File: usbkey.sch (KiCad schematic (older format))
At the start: 15 parts, among them P1 USART0, P2 DEBUG, P3 USB_B, U1 EFM32HG309

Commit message: Give all the nets names.
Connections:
- net LED1: now reaches R1.1, U1.1 (PA0)
- net DEC: now reaches C1.2, U1.14 (DECOUPLE)
- net RUSB_D+: now reaches R3.2, U1.17 (PC14)
- net RUSB_D-: now reaches R4.2, U1.18 (PC15)
- net CAP1: now reaches U1.23 (PE12), U1.4 (PC1), W2.2
- net CAP0: now reaches U1.24 (PE13), U1.3 (PC0), W1.2
- net US0_TX: now reaches P1.3 (P3), U1.5 (PB7)
- net US0_RX: now reaches P1.2 (P2), U1.6 (PB8)
- net LED0: now reaches R2.2, U1.8 (PB11)
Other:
- note removed: "US0_RX"
- note removed: "US0_TX\n"
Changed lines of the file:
@@
 EESchema Schematic File Version 2
+LIBS:usbkey-rescue
 LIBS:power
 LIBS:device
@@
 P 5725 4025
 F 0 "C1" V 5675 4075 50  0000 L CNN
-F 1 "1uF" V 5675 3850 50  0000 L CNN
+F 1 "1uF" V 5775 4075 50  0000 L CNN
 F 2 "Capacitors_SMD:C_0402" H 5725 4025 50  0001 C CNN
 F 3 "" H 5725 4025 50  0000 C CNN
@@
 	1    0    0    -1
 $EndComp
-Text Notes 2450 3075 0    39   ~ 0
-US0_TX\n
-Text Notes 2450 3175 0    39   ~ 0
-US0_RX
 Wire Wire Line
 	4175 3025 4200 3025
@@
 	4025 3775 4200 3775
 Connection ~ 4025 3625
+Text Label 3850 3425 0    39   ~ 0
+CAP0
+Text Label 3850 3625 0    39   ~ 0
+CAP1
+Text Label 2775 3075 0    39   ~ 0
+US0_TX
+Text Label 2775 3175 0    39   ~ 0
+US0_RX
+Text Label 5550 4025 0    39   ~ 0
+DEC
+Text Label 4175 2600 1    39   ~ 0
+LED1
+Text Label 4050 2600 1    39   ~ 0
+LED0
+Text Label 5500 3100 0    8    ~ 0
+RUSB_D+
+Text Label 5500 3175 0    8    ~ 0
+RUSB_D-
 $EndSCHEMATC

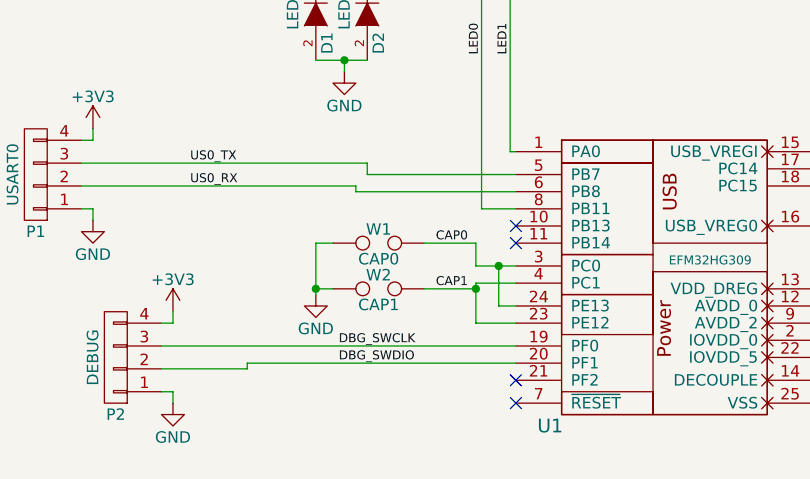
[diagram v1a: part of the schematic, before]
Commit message: Playing with things.
ADC on one side, capacitive on the other.

Starting on USB PCB component.
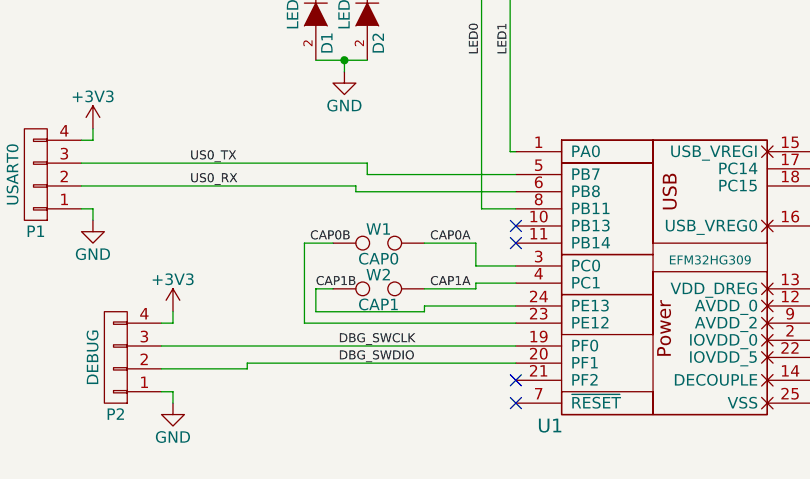
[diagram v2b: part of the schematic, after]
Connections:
- net GND: no longer W1.1, W2.1
- net CAP0 renamed CAP0A
- net CAP0A: no longer U1.24 (PE13)
- net CAP1 renamed CAP1A
- net CAP1A: no longer U1.23 (PE12)
- new net CAP0B: U1.23 (PE12), W1.1
- new net CAP1B: U1.24 (PE13), W2.1
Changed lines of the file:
@@
 $EndComp
 $Comp
-L GND #PWR8
+L GND #PWR01
 U 1 1 5798BA02
 P 6200 4175
-F 0 "#PWR8" H 6200 3925 50  0001 C CNN
+F 0 "#PWR01" H 6200 3925 50  0001 C CNN
 F 1 "GND" H 6200 4025 50  0000 C CNN
 F 2 "" H 6200 4175 50  0000 C CNN
@@
 	2700 4075 2700 4125
 $Comp
-L GND #PWR4
+L GND #PWR02
 U 1 1 5798EEB6
 P 2700 4125
-F 0 "#PWR4" H 2700 3875 50  0001 C CNN
+F 0 "#PWR02" H 2700 3875 50  0001 C CNN
 F 1 "GND" H 2700 3975 50  0000 C CNN
 F 2 "" H 2700 4125 50  0000 C CNN
@@
 	2700 3775 2700 3725
 $Comp
-L +3V3 #PWR7
+L +3V3 #PWR03
 U 1 1 5798EF1D
 P 6000 3575
-F 0 "#PWR7" H 6000 3425 50  0001 C CNN
+F 0 "#PWR03" H 6000 3425 50  0001 C CNN
 F 1 "+3V3" H 6000 3715 50  0000 C CNN
 F 2 "" H 6000 3575 50  0000 C CNN
@@
 Connection ~ 6350 4125
 $Comp
-L +3V3 #PWR3
+L +3V3 #PWR04
 U 1 1 5798F04E
 P 2700 3725
-F 0 "#PWR3" H 2700 3575 50  0001 C CNN
+F 0 "#PWR04" H 2700 3575 50  0001 C CNN
 F 1 "+3V3" H 2700 3865 50  0000 C CNN
 F 2 "" H 2700 3725 50  0000 C CNN
@@
 $EndComp
 $Comp
-L GND #PWR6
+L GND #PWR05
 U 1 1 5798FAA2
 P 3450 2675
-F 0 "#PWR6" H 3450 2425 50  0001 C CNN
+F 0 "#PWR05" H 3450 2425 50  0001 C CNN
 F 1 "GND" H 3450 2525 50  0000 C CNN
 F 2 "" H 3450 2675 50  0000 C CNN
@@
 	2350 3275 2350 3325
 $Comp
-L GND #PWR2
+L GND #PWR06
 U 1 1 5798FD6B
 P 2350 3325
-F 0 "#PWR2" H 2350 3075 50  0001 C CNN
+F 0 "#PWR06" H 2350 3075 50  0001 C CNN
 F 1 "GND" H 2350 3175 50  0000 C CNN
 F 2 "" H 2350 3325 50  0000 C CNN
@@
 	2350 2975 2350 2925
 $Comp
-L +3V3 #PWR1
+L +3V3 #PWR07
 U 1 1 5798FD73
 P 2350 2925
-F 0 "#PWR1" H 2350 2775 50  0001 C CNN
+F 0 "#PWR07" H 2350 2775 50  0001 C CNN
 F 1 "+3V3" H 2350 3065 50  0000 C CNN
 F 2 "" H 2350 2925 50  0000 C CNN
@@
 	1    0    0    -1
 $EndComp
-$Comp
-L GND #PWR5
-U 1 1 57990607
-P 3325 3650
-F 0 "#PWR5" H 3325 3400 50  0001 C CNN
-F 1 "GND" H 3325 3500 50  0000 C CNN
-F 2 "" H 3325 3650 50  0000 C CNN
-F 3 "" H 3325 3650 50  0000 C CNN
-	1    3325 3650
-	1    0    0    -1
-$EndComp
-Wire Wire Line
-	3325 3425 3325 3650
 Wire Wire Line
 	3325 3625 3400 3625
 Wire Wire Line
-	3325 3425 3400 3425
-Connection ~ 3325 3625
+	3275 3425 3400 3425
 Wire Wire Line
 	3800 3425 4025 3425
@@
 Wire Wire Line
 	4200 3600 4025 3600
-Wire Wire Line
-	4025 3600 4025 3775
 Wire Wire Line
 	4025 3625 3800 3625
@@
 NoConn ~ 4200 3350
 Wire Wire Line
-	4200 3700 4125 3700
-Wire Wire Line
-	4125 3700 4125 3525
-Connection ~ 4125 3525
-Wire Wire Line
-	4025 3775 4200 3775
-Connection ~ 4025 3625
-Text Label 3850 3425 0    39   ~ 0
-CAP0
-Text Label 3850 3625 0    39   ~ 0
-CAP1
+	3800 3700 4200 3700
+Wire Wire Line
+	3275 3775 4200 3775
+Text Label 3825 3425 0    39   ~ 0
+CAP0A
+Text Label 3825 3625 0    39   ~ 0
+CAP1A
 Text Label 2775 3075 0    39   ~ 0
 US0_TX
@@
 Text Label 5500 3175 0    8    ~ 0
 RUSB_D-
+Wire Wire Line
+	4025 3600 4025 3625
+Wire Wire Line
+	3800 3700 3800 3725
+Wire Wire Line
+	3800 3725 3325 3725
+Wire Wire Line
+	3325 3725 3325 3625
+Wire Wire Line
+	3275 3775 3275 3425
+Text Label 3300 3425 0    39   ~ 0
+CAP0B
+Text Label 3325 3625 0    39   ~ 0
+CAP1B
 $EndSCHEMATC

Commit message: Temp commit.
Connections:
- net DBG_SWCLK: now also P2.2 (P2); no longer P2.3 (P3)
- net DBG_SWDIO: now also P2.3 (P3); no longer P2.2 (P2)
- net GND: no longer P3.5 (shield)
- net RUSB_D+: now also R4.2, U1.18 (PC15); no longer R3.2, U1.17 (PC14)
- net RUSB_D-: now also R3.2, U1.17 (PC14); no longer R4.2, U1.18 (PC15)
- net USB_D+: now also P3.3 (D+), R4.1; no longer P3.2 (D-), R3.1
- net USB_D-: now also P3.2 (D-), R3.1; no longer P3.3 (D+), R4.1
- no-connect marks 4 -> 5
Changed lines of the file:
@@
 EESchema Schematic File Version 2
-LIBS:usbkey-rescue
 LIBS:power
 LIBS:device
@@
 $EndComp
 Text Label 5825 3100 0    39   ~ 0
+USB_D-
+Text Label 5825 3175 0    39   ~ 0
 USB_D+
-Text Label 5825 3175 0    39   ~ 0
-USB_D-
 Text Label 5825 3350 0    39   ~ 0
 VCC3V3
@@
 Connection ~ 6125 4125
 Wire Wire Line
-	6750 4125 6750 3525
-Wire Wire Line
 	6125 3350 6125 3875
 Wire Wire Line
@@
 Wire Wire Line
 	7000 4125 7000 3950
-Connection ~ 6750 4125
 Wire Wire Line
 	7000 3750 7000 2875
@@
 Connection ~ 5950 4125
 Wire Wire Line
-	2650 3875 4200 3875
-Wire Wire Line
-	3025 3950 4200 3950
-Wire Wire Line
-	3025 3950 3025 3975
-Wire Wire Line
-	3025 3975 2650 3975
+	3025 3875 4200 3875
+Wire Wire Line
+	2825 3950 4200 3950
 Wire Wire Line
 	2650 4075 2700 4075
@@
 LED0
 Text Label 5500 3100 0    8    ~ 0
+RUSB_D-
+Text Label 5500 3175 0    8    ~ 0
 RUSB_D+
-Text Label 5500 3175 0    8    ~ 0
-RUSB_D-
 Wire Wire Line
 	4025 3600 4025 3625
@@
 Text Label 3325 3625 0    39   ~ 0
 CAP1B
+Wire Wire Line
+	2825 3950 2825 3875
+Wire Wire Line
+	2825 3875 2650 3875
+Wire Wire Line
+	3025 3875 3025 3975
+Wire Wire Line
+	3025 3975 2650 3975
+NoConn ~ 6750 3525
 $EndSCHEMATC

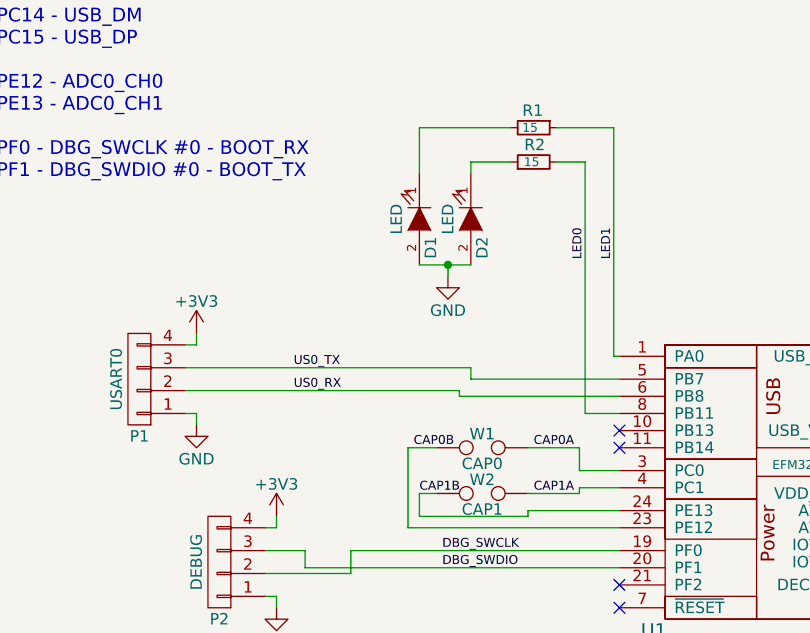
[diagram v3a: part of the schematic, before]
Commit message: Lots of modifications.
Trying to make 5mil/5mil pass.
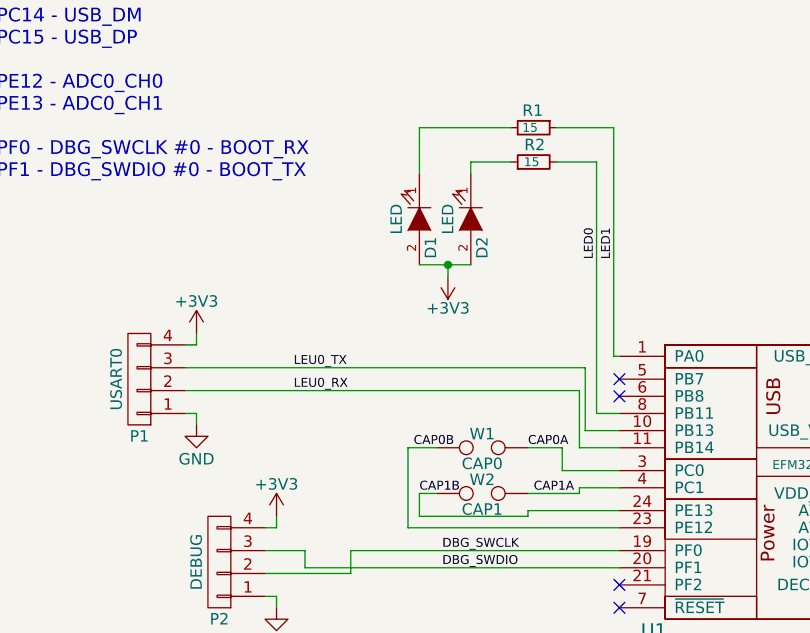
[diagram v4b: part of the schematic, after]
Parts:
- P3: footprint Connect:USB_B -> usb-pcb:USB-PCB
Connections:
- net +3V3: now also D1.2 (A), D2.2 (A)
- net GND: no longer D1.2 (A), D2.2 (A)
- net LEU0_TX: now reaches U1.10 (PB13)
- net LEU0_TX: now also P1.3 (P3)
- net LEU0_RX: now reaches U1.11 (PB14)
- net LEU0_RX: now also P1.2 (P2)
- net US0_RX: no longer names the net of U1.6 (PB8)
- net US0_RX: no longer P1.2 (P2)
- net US0_TX: no longer names the net of U1.5 (PB7)
- net US0_TX: no longer P1.3 (P3)
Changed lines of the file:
@@
 F 0 "P3" H 6850 3025 50  0000 C CNN
 F 1 "USB_B" H 6600 3425 50  0000 C CNN
-F 2 "Connect:USB_B" V 6600 3125 50  0001 C CNN
+F 2 "usb-pcb:USB-PCB" V 6600 3125 50  0001 C CNN
 F 3 "" V 6600 3125 50  0000 C CNN
 	1    6650 3225
@@
 	0    1    1    0
 $EndComp
-$Comp
-L GND #PWR05
-U 1 1 5798FAA2
-P 3450 2675
-F 0 "#PWR05" H 3450 2425 50  0001 C CNN
-F 1 "GND" H 3450 2525 50  0000 C CNN
-F 2 "" H 3450 2675 50  0000 C CNN
-F 3 "" H 3450 2675 50  0000 C CNN
-	1    3450 2675
-	1    0    0    -1
-$EndComp
 Wire Wire Line
 	3450 2675 3450 2625
@@
 	2350 3275 2350 3325
 $Comp
-L GND #PWR06
+L GND #PWR05
 U 1 1 5798FD6B
 P 2350 3325
-F 0 "#PWR06" H 2350 3075 50  0001 C CNN
+F 0 "#PWR05" H 2350 3075 50  0001 C CNN
 F 1 "GND" H 2350 3175 50  0000 C CNN
 F 2 "" H 2350 3325 50  0000 C CNN
@@
 	2350 2975 2350 2925
 $Comp
-L +3V3 #PWR07
+L +3V3 #PWR06
 U 1 1 5798FD73
 P 2350 2925
-F 0 "#PWR07" H 2350 2775 50  0001 C CNN
+F 0 "#PWR06" H 2350 2775 50  0001 C CNN
 F 1 "+3V3" H 2350 3065 50  0000 C CNN
 F 2 "" H 2350 2925 50  0000 C CNN
@@
 	3275 3425 3400 3425
 Wire Wire Line
-	3800 3425 4025 3425
-Wire Wire Line
-	4025 3425 4025 3525
-Wire Wire Line
-	4025 3525 4200 3525
+	3800 3425 3950 3425
+Wire Wire Line
+	3950 3425 3950 3525
+Wire Wire Line
+	3950 3525 4200 3525
 Wire Wire Line
 	4200 3600 4025 3600
@@
 	4175 2025 3925 2025
 Wire Wire Line
-	4200 3125 3550 3125
-Wire Wire Line
-	3550 3125 3550 3075
-Wire Wire Line
-	3550 3075 2300 3075
-Wire Wire Line
-	4200 3200 3500 3200
-Wire Wire Line
-	3500 3200 3500 3175
-Wire Wire Line
-	3500 3175 2300 3175
-Wire Wire Line
-	4200 3275 4050 3275
-Wire Wire Line
-	4050 3275 4050 2175
-Wire Wire Line
-	4050 2175 3925 2175
+	2300 3075 4050 3075
+Wire Wire Line
+	2300 3175 4025 3175
+Wire Wire Line
+	4200 3275 4100 3275
+Wire Wire Line
+	4100 3275 4100 2175
+Wire Wire Line
+	4100 2175 3925 2175
 NoConn ~ 4200 4125
 NoConn ~ 4200 4025
-NoConn ~ 4200 3425
-NoConn ~ 4200 3350
 Wire Wire Line
 	3800 3700 4200 3700
 Wire Wire Line
 	3275 3775 4200 3775
-Text Label 3825 3425 0    39   ~ 0
+Text Label 3800 3425 0    39   ~ 0
 CAP0A
 Text Label 3825 3625 0    39   ~ 0
 CAP1A
 Text Label 2775 3075 0    39   ~ 0
-US0_TX
+LEU0_TX
 Text Label 2775 3175 0    39   ~ 0
-US0_RX
+LEU0_RX
 Text Label 5550 4025 0    39   ~ 0
 DEC
 Text Label 4175 2600 1    39   ~ 0
 LED1
-Text Label 4050 2600 1    39   ~ 0
+Text Label 4100 2600 1    39   ~ 0
 LED0
 Text Label 5500 3100 0    8    ~ 0
@@
 	3025 3975 2650 3975
 NoConn ~ 6750 3525
+$Comp
+L +3V3 #PWR07
+U 1 1 579B6568
+P 3450 2675
+F 0 "#PWR07" H 3450 2525 50  0001 C CNN
+F 1 "+3V3" H 3450 2815 50  0000 C CNN
+F 2 "" H 3450 2675 50  0000 C CNN
+F 3 "" H 3450 2675 50  0000 C CNN
+	1    3450 2675
+	-1   0    0    1
+$EndComp
+Wire Wire Line
+	4200 3350 4050 3350
+Wire Wire Line
+	4050 3350 4050 3075
+Wire Wire Line
+	4200 3425 4025 3425
+Wire Wire Line
+	4025 3425 4025 3175
+NoConn ~ 4200 3200
+NoConn ~ 4200 3125
 $EndSCHEMATC

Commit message: Lots more work.
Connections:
- net LED0: now also U1.5 (PB7); no longer U1.8 (PB11)
- no-connect marks 5 -> 3
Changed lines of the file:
@@
-$EndComp
-$Comp
-L EFM32HG309 U1
-U 1 1 5798B6D7
-P 4400 4175
-F 0 "U1" H 4350 4125 60  0000 C CNN
-F 1 "EFM32HG309" H 5050 4850 39  0000 C CNN
-F 2 "Housings_DFN_QFN:QFN-24-1EP_5x5mm_Pitch0.65mm" H 4400 4175 60  0001 C CNN
-F 3 "" H 4400 4175 60  0000 C CNN
-	1    4400 4175
-	1    0    0    -1
 $EndComp
 $Comp
@@
 Text Label 3425 3950 0    39   ~ 0
 DBG_SWDIO
-Wire Wire Line
-	5500 3350 6125 3350
-Wire Wire Line
-	5750 3625 5500 3625
-Connection ~ 5750 3350
-Connection ~ 5750 3625
-Wire Wire Line
-	6200 4125 6200 4175
-Wire Wire Line
-	6125 4125 6125 4075
-Connection ~ 6200 4125
-Wire Wire Line
-	5950 4025 5950 4125
-Connection ~ 6125 4125
-Wire Wire Line
-	6125 3350 6125 3875
-Wire Wire Line
-	5750 3350 5750 3925
-Wire Wire Line
-	5550 3100 5500 3100
-Wire Wire Line
-	5500 3175 5550 3175
-Wire Wire Line
-	5500 3025 6350 3025
-Wire Wire Line
-	5750 3100 6200 3100
-Wire Wire Line
-	6350 3125 6200 3125
-Wire Wire Line
-	6200 3125 6200 3100
-Wire Wire Line
-	6350 3225 6200 3225
-Wire Wire Line
-	6200 3225 6200 3175
-Wire Wire Line
-	6200 3175 5750 3175
-Wire Wire Line
-	5500 4125 7000 4125
-Wire Wire Line
-	7000 4125 7000 3950
-Wire Wire Line
-	7000 3750 7000 2875
-Wire Wire Line
-	7000 2875 6300 2875
-Wire Wire Line
-	6300 2875 6300 3025
-Connection ~ 6300 3025
-Wire Wire Line
-	5750 3700 5500 3700
-Wire Wire Line
-	5750 3775 5500 3775
-Connection ~ 5750 3700
-Wire Wire Line
-	5750 3850 5500 3850
-Connection ~ 5750 3775
-Wire Wire Line
-	5750 3925 5500 3925
-Connection ~ 5750 3850
-Wire Wire Line
-	5500 4025 5625 4025
-Wire Wire Line
-	5825 4025 5950 4025
-Connection ~ 5950 4125
-Wire Wire Line
-	3025 3875 4200 3875
-Wire Wire Line
-	2825 3950 4200 3950
-Wire Wire Line
-	2650 4075 2700 4075
-Wire Wire Line
-	2700 4075 2700 4125
 $Comp
 L GND #PWR02
@@
 	1    0    0    -1
 $EndComp
-Wire Wire Line
-	2650 3775 2700 3775
-Wire Wire Line
-	2700 3775 2700 3725
 $Comp
 L +3V3 #PWR03
@@
 	1    0    0    -1
 $EndComp
-Wire Wire Line
-	6000 3575 6000 3625
-Wire Wire Line
-	6000 3625 6125 3625
-Connection ~ 6125 3625
-Wire Wire Line
-	6350 3325 6350 4125
-Connection ~ 6350 4125
 $Comp
 L +3V3 #PWR04
@@
 	0    1    1    0
 $EndComp
-Wire Wire Line
-	3450 2675 3450 2625
-Wire Wire Line
-	3325 2625 3550 2625
-Connection ~ 3450 2625
-Wire Wire Line
-	3725 2175 3550 2175
-Wire Wire Line
-	3550 2175 3550 2225
-Wire Wire Line
-	3725 2025 3325 2025
-Wire Wire Line
-	3325 2025 3325 2225
 $Comp
 L CONN_01X04 P1
@@
 	-1   0    0    1
 $EndComp
-Wire Wire Line
-	2300 3275 2350 3275
-Wire Wire Line
-	2350 3275 2350 3325
 $Comp
 L GND #PWR05
@@
 	1    0    0    -1
 $EndComp
-Wire Wire Line
-	2300 2975 2350 2975
-Wire Wire Line
-	2350 2975 2350 2925
 $Comp
 L +3V3 #PWR06
@@
 	1    0    0    -1
 $EndComp
-Wire Wire Line
-	4175 3025 4200 3025
-Wire Wire Line
-	4175 2025 4175 3025
 $Comp
 L TEST W1
@@
 	1    0    0    -1
 $EndComp
-Wire Wire Line
-	3325 3625 3400 3625
-Wire Wire Line
-	3275 3425 3400 3425
-Wire Wire Line
-	3800 3425 3950 3425
-Wire Wire Line
-	3950 3425 3950 3525
-Wire Wire Line
-	3950 3525 4200 3525
-Wire Wire Line
-	4200 3600 4025 3600
-Wire Wire Line
-	4025 3625 3800 3625
 Text Notes 1475 2350 0    60   ~ 0
 PB8 - US0_RX\nPB7 - US0_TX\n\nPA0 - Timer 0 Capture Compare Channel 0 -- For PWM - LED0 \nPB7 - Timer 1 Capture Compare Channel 0 -- For PWM - LED1\n\nPC0 - ACMP0_CH0 - Capacitive Touch 0\nPC1 - ACMP0_CH1 - Capacitive Touch 1\n\nPC14 - USB_DM\nPC15 - USB_DP\n\nPE12 - ADC0_CH0\nPE13 - ADC0_CH1\n\nPF0 - DBG_SWCLK #0 - BOOT_RX\nPF1 - DBG_SWDIO #0 - BOOT_TX\n\n
-Wire Wire Line
-	4175 2025 3925 2025
-Wire Wire Line
-	2300 3075 4050 3075
-Wire Wire Line
-	2300 3175 4025 3175
-Wire Wire Line
-	4200 3275 4100 3275
-Wire Wire Line
-	4100 3275 4100 2175
-Wire Wire Line
-	4100 2175 3925 2175
 NoConn ~ 4200 4125
 NoConn ~ 4200 4025
-Wire Wire Line
-	3800 3700 4200 3700
-Wire Wire Line
-	3275 3775 4200 3775
 Text Label 3800 3425 0    39   ~ 0
 CAP0A
@@
 Text Label 5500 3175 0    8    ~ 0
 RUSB_D+
-Wire Wire Line
-	4025 3600 4025 3625
-Wire Wire Line
-	3800 3700 3800 3725
-Wire Wire Line
-	3800 3725 3325 3725
-Wire Wire Line
-	3325 3725 3325 3625
-Wire Wire Line
-	3275 3775 3275 3425
 Text Label 3300 3425 0    39   ~ 0
 CAP0B
 Text Label 3325 3625 0    39   ~ 0
 CAP1B
-Wire Wire Line
-	2825 3950 2825 3875
-Wire Wire Line
-	2825 3875 2650 3875
-Wire Wire Line
-	3025 3875 3025 3975
-Wire Wire Line
-	3025 3975 2650 3975
 NoConn ~ 6750 3525
 $Comp
@@
 	-1   0    0    1
 $EndComp
+$Comp
+L EFM32HG309 U1
+U 1 1 5798B6D7
+P 4400 4175
+F 0 "U1" H 4350 4125 60  0000 C CNN
+F 1 "EFM32HG309" H 5050 4850 39  0000 C CNN
+F 2 "Housings_DFN_QFN:QFN-24-1EP_5x5mm_Pitch0.65mm" H 4400 4175 60  0001 C CNN
+F 3 "" H 4400 4175 60  0000 C CNN
+	1    4400 4175
+	1    0    0    -1
+$EndComp
+Wire Wire Line
+	5500 3350 6125 3350
+Wire Wire Line
+	5750 3625 5500 3625
+Connection ~ 5750 3350
+Connection ~ 5750 3625
+Wire Wire Line
+	6200 4125 6200 4175
+Wire Wire Line
+	6125 4125 6125 4075
+Connection ~ 6200 4125
+Wire Wire Line
+	5950 4025 5950 4125
+Connection ~ 6125 4125
+Wire Wire Line
+	6125 3350 6125 3875
+Wire Wire Line
+	5750 3350 5750 3925
+Wire Wire Line
+	5550 3100 5500 3100
+Wire Wire Line
+	5500 3175 5550 3175
+Wire Wire Line
+	5500 3025 6350 3025
+Wire Wire Line
+	5750 3100 6200 3100
+Wire Wire Line
+	6350 3125 6200 3125
+Wire Wire Line
+	6200 3125 6200 3100
+Wire Wire Line
+	6350 3225 6200 3225
+Wire Wire Line
+	6200 3225 6200 3175
+Wire Wire Line
+	6200 3175 5750 3175
+Wire Wire Line
+	5500 4125 7000 4125
+Wire Wire Line
+	7000 4125 7000 3950
+Wire Wire Line
+	7000 3750 7000 2875
+Wire Wire Line
+	7000 2875 6300 2875
+Wire Wire Line
+	6300 2875 6300 3025
+Connection ~ 6300 3025
+Wire Wire Line
+	5750 3700 5500 3700
+Wire Wire Line
+	5750 3775 5500 3775
+Connection ~ 5750 3700
+Wire Wire Line
+	5750 3850 5500 3850
+Connection ~ 5750 3775
+Wire Wire Line
+	5750 3925 5500 3925
+Connection ~ 5750 3850
+Wire Wire Line
+	5500 4025 5625 4025
+Wire Wire Line
+	5825 4025 5950 4025
+Connection ~ 5950 4125
+Wire Wire Line
+	3025 3875 4200 3875
+Wire Wire Line
+	2825 3950 4200 3950
+Wire Wire Line
+	2650 4075 2700 4075
+Wire Wire Line
+	2700 4075 2700 4125
+Wire Wire Line
+	2650 3775 2700 3775
+Wire Wire Line
+	2700 3775 2700 3725
+Wire Wire Line
+	6000 3575 6000 3625
+Wire Wire Line
+	6000 3625 6125 3625
+Connection ~ 6125 3625
+Wire Wire Line
+	6350 3325 6350 4125
+Connection ~ 6350 4125
+Wire Wire Line
+	3450 2675 3450 2625
+Wire Wire Line
+	3325 2625 3550 2625
+Connection ~ 3450 2625
+Wire Wire Line
+	3725 2175 3550 2175
+Wire Wire Line
+	3550 2175 3550 2225
+Wire Wire Line
+	3725 2025 3325 2025
+Wire Wire Line
+	3325 2025 3325 2225
+Wire Wire Line
+	2300 3275 2350 3275
+Wire Wire Line
+	2350 3275 2350 3325
+Wire Wire Line
+	2300 2975 2350 2975
+Wire Wire Line
+	2350 2975 2350 2925
+Wire Wire Line
+	4175 2025 4175 3025
+Wire Wire Line
+	3325 3625 3400 3625
+Wire Wire Line
+	3275 3425 3400 3425
+Wire Wire Line
+	3800 3425 3950 3425
+Wire Wire Line
+	3950 3425 3950 3525
+Wire Wire Line
+	3950 3525 4200 3525
+Wire Wire Line
+	4200 3600 4025 3600
+Wire Wire Line
+	4025 3625 3800 3625
+Wire Wire Line
+	4175 2025 3925 2025
+Wire Wire Line
+	2300 3075 4050 3075
+Wire Wire Line
+	2300 3175 4025 3175
+Wire Wire Line
+	4100 3125 4100 2175
+Wire Wire Line
+	4100 2175 3925 2175
+Wire Wire Line
+	3800 3700 4200 3700
+Wire Wire Line
+	3275 3775 4200 3775
+Wire Wire Line
+	4025 3600 4025 3625
+Wire Wire Line
+	3800 3700 3800 3725
+Wire Wire Line
+	3800 3725 3325 3725
+Wire Wire Line
+	3325 3725 3325 3625
+Wire Wire Line
+	3275 3775 3275 3425
+Wire Wire Line
+	2825 3950 2825 3875
+Wire Wire Line
+	2825 3875 2650 3875
+Wire Wire Line
+	3025 3875 3025 3975
+Wire Wire Line
+	3025 3975 2650 3975
 Wire Wire Line
 	4200 3350 4050 3350
@@
 Wire Wire Line
 	4025 3425 4025 3175
-NoConn ~ 4200 3200
-NoConn ~ 4200 3125
+Wire Wire Line
+	4175 3025 4200 3025
+Wire Wire Line
+	4100 3125 4200 3125
 $EndSCHEMATC

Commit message: Small cleanup.
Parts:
- P3: value USB_B -> USB_PCB; symbol USB_B -> USB_PCB
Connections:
- no-connect marks 3 -> 2
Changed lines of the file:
@@
 EESchema Schematic File Version 2
+LIBS:usbkey-rescue
 LIBS:power
 LIBS:device
@@
 LIBS:valves
 LIBS:efm32hg309
+LIBS:usb_pcb
 LIBS:usbkey-cache
 EELAYER 25 0
@@
 Sheet 1 1
 Title ""
-Date ""
+Date "$Id$"
 Rev ""
 Comp ""
-Comment1 ""
+Comment1 "License: CC-BY-SA 4.0 or TAPR"
 Comment2 ""
 Comment3 ""
@@
 $EndComp
 $Comp
-L USB_B P3
+L USB_PCB P3
 U 1 1 5798BECB
 P 6650 3225
 F 0 "P3" H 6850 3025 50  0000 C CNN
-F 1 "USB_B" H 6600 3425 50  0000 C CNN
+F 1 "USB_PCB" H 6600 3425 50  0000 C CNN
 F 2 "usb-pcb:USB-PCB" V 6600 3125 50  0001 C CNN
 F 3 "" V 6600 3125 50  0000 C CNN
@@
 Text Label 3325 3625 0    39   ~ 0
 CAP1B
-NoConn ~ 6750 3525
 $Comp
 L +3V3 #PWR07
